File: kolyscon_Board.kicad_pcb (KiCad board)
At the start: 2 copper layers, 47 parts, among them J1 Conn_01x04, Q1 HL2302, Q10 HL2302, Q11 HL2302, Q2 HL2302, Q3 HL2302, Q4 HL2302, Q5 HL2302, Q6 HL2302, Q7 HL2302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

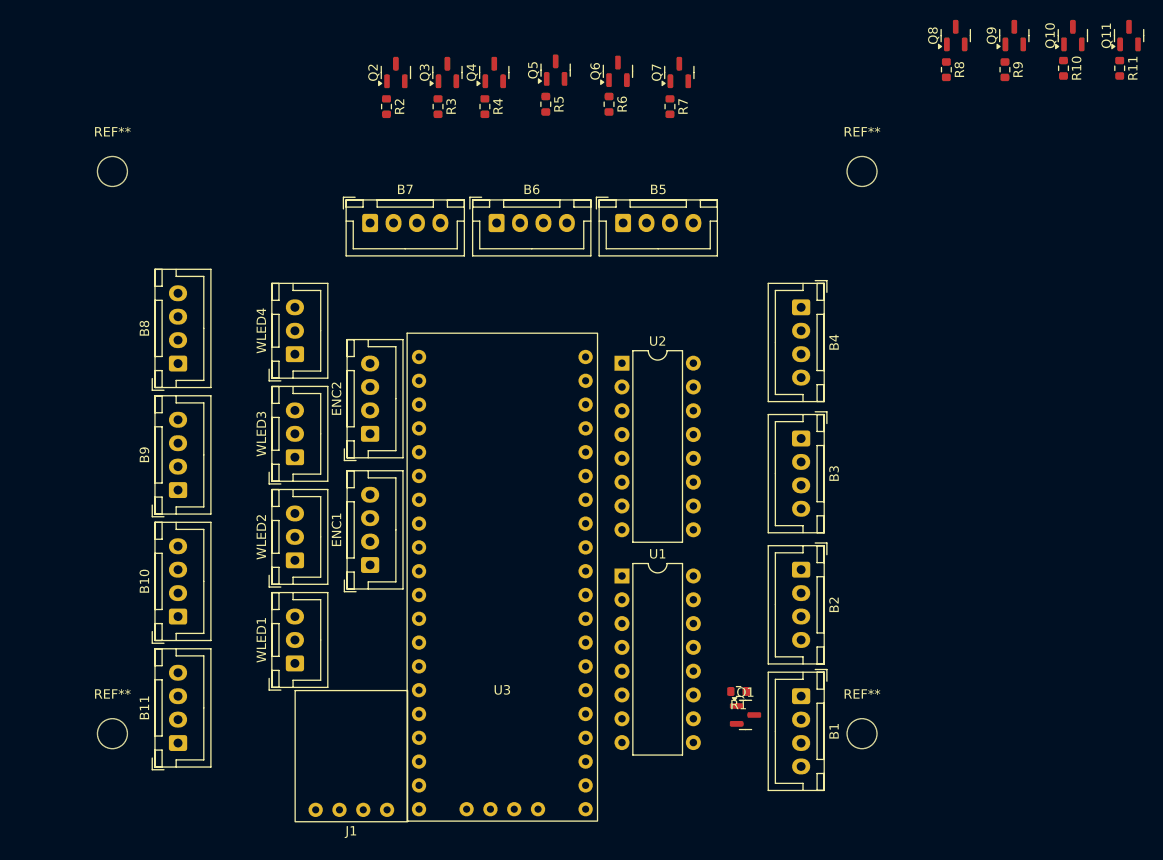
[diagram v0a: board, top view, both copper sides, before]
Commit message: Schema work
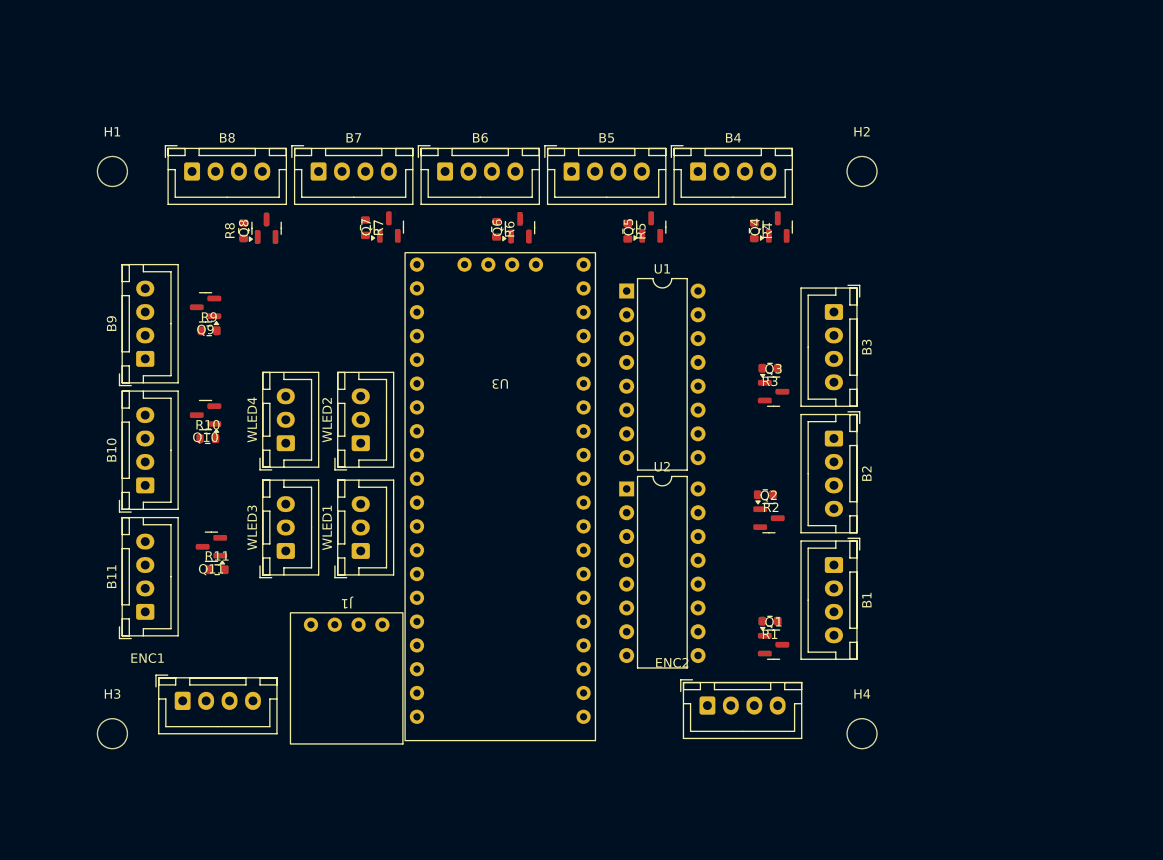
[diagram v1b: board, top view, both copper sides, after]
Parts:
- removed REF** (x4): MountingHole_3.2mm_M3, MountingHole:MountingHole_3.2mm_M3
- added H1: MountingHole, MountingHole:MountingHole_3.2mm_M3, F.Cu at (70.0, 70.0)
- added H2: MountingHole, MountingHole:MountingHole_3.2mm_M3, F.Cu at (150.0, 70.0)
- added H3: MountingHole, MountingHole:MountingHole_3.2mm_M3, F.Cu at (70.0, 130.0)
- added H4: MountingHole, MountingHole:MountingHole_3.2mm_M3, F.Cu at (150.0, 130.0)
- moved Q11 112.1 mm to (80.6, 110.0), turned to 180 degrees
- moved R11 110.2 mm to (81.2, 112.5), turned to 0 degrees
- moved Q10 101.0 mm to (79.9, 96.0), turned to 180 degrees
- moved R10 99.5 mm to (80.2, 98.5), turned to 0 degrees
- moved Q9 91.1 mm to (79.9, 84.5), turned to 180 degrees
- moved R9 89.4 mm to (80.3, 87.0), turned to 0 degrees
- moved R8 76.9 mm to (84.0, 76.3), turned to 90 degrees
- moved Q8 76.4 mm to (86.5, 76.1)
- moved Q2 62.0 mm to (140.1, 107.0), turned to 0 degrees
- moved U3 60.7 mm to (111.4, 78.7), turned to 180 degrees
- moved R2 57.9 mm to (139.7, 104.5), turned to 180 degrees
- moved Q3 48.7 mm to (140.6, 93.5), turned to 0 degrees
- moved ENC2 46.2 mm to (133.5, 127.0), turned to 0 degrees
- moved R3 45.1 mm to (140.2, 91.0), turned to 180 degrees
- moved Q7 35.1 mm to (99.5, 75.9)
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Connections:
- J1 pad 1: GND -> GND_PWR
- WLED1 pad 1: GND -> GND_PWR
- WLED2 pad 1: GND -> GND_PWR
- WLED3 pad 1: GND -> GND_PWR
- WLED4 pad 1: GND -> GND_PWR

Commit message: -Routing
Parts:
- added G***: LOGO, kolyscon_Board_Footprints:konmai, F.Cu at (92.0, 83.0)
- Q1, Q10, Q11, Q2, Q3, Q4, Q5, Q6, Q7, Q8, Q9: value HL2302 -> ~
- R1, R10, R11, R2, R3, R4, R5, R6, R7, R8, R9: value R -> R1k
- moved WLED4 8.63 mm to (97.0, 97.5)
- moved WLED3 8.50 mm to (97.0, 110.5)
- moved WLED2 7.65 mm to (89.0, 97.5)
- moved WLED1 7.50 mm to (89.0, 110.5)
- moved Q9 3.25 mm to (79.9, 81.2)
- moved R9 3.25 mm to (80.3, 83.8)
- moved B1 2.50 mm to (147.0, 109.5)
- moved B2 2.50 mm to (147.0, 96.0)
- moved B3 2.50 mm to (147.0, 82.5)
- moved Q1 2.50 mm to (140.6, 118.0)
- moved Q2 2.50 mm to (140.1, 104.5)
- moved Q3 2.50 mm to (140.6, 91.0)
- moved R1 2.50 mm to (140.2, 115.5)
- moved R2 2.50 mm to (139.7, 102.0)
- moved R3 2.50 mm to (140.2, 88.5)
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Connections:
- J1 pad 1: GND_PWR -> GND
- U3 pad 10: /BT_D_6 -> /BT_D_2
- U3 pad 11: /BT_D_7 -> /BT_D_3
- U3 pad 12: /BT_D_8 -> /BT_D_4
- U3 pad 13: /BT_D_9 -> /BT_D_7
- U3 pad 14: /BT_D_10 -> /BT_D_6
- U3 pad 15: unconnected-(U3-GND-Pad15) -> GND
- U3 pad 16: /BT_D_11 -> /BT_D_5
- U3 pad 25: /WLED_1 -> /BT_D_8
- U3 pad 26: /WLED_2 -> /BT_D_9
- U3 pad 27: /WLED_3 -> /BT_D_10
- U3 pad 28: /WLED_4 -> /BT_D_11
- U3 pad 29: /ENC_1_A -> /WLED_1
- U3 pad 30: /ENC_1_B -> /WLED_2
- U3 pad 31: /ENC_2_A -> /WLED_3
- U3 pad 32: /ENC_2_B -> /WLED_4
- U3 pad 4: /BT_D_1 -> /ENC_1_A
- U3 pad 5: /BT_D_2 -> /ENC_1_B
- U3 pad 6: unconnected-(U3-GND-Pad6) -> GND
- U3 pad 7: /BT_D_4 -> /ENC_2_A
- U3 pad 8: /BT_D_3 -> /ENC_2_B
- U3 pad 9: /BT_D_5 -> /BT_D_1
- WLED1 pad 1: GND_PWR -> GND
- WLED2 pad 1: GND_PWR -> GND
- WLED3 pad 1: GND_PWR -> GND
- WLED4 pad 1: GND_PWR -> GND
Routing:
- net GND: track 0.00 -> 486.9 mm
- net +5V: track 0.00 -> 348.2 mm, vias 0 -> 2
- net /BT_L_9: track 0.00 -> 62.5 mm, vias 0 -> 2
- net /BT_D_11: track 0.00 -> 52.4 mm
- net /BT_L_11: track 0.00 -> 49.6 mm, vias 0 -> 1
- net /BT_L_8: track 0.00 -> 48.7 mm, vias 0 -> 2
- net /SHIFTREG_SER: track 0.00 -> 48.6 mm
- net /BT_L_10: track 0.00 -> 48.0 mm, vias 0 -> 3
- net /SHIFTREG_LATCH: track 0.00 -> 45.8 mm, vias 0 -> 2
- net /BT_D_7: track 0.00 -> 45.7 mm
- net /ENC_1_A: track 0.00 -> 45.6 mm, vias 0 -> 1
- net /ENC_1_B: track 0.00 -> 43.8 mm
- net +5V_PWR: track 0.00 -> 43.6 mm
- net /SHIFTREG_CLK: track 0.00 -> 43.5 mm, vias 0 -> 2
- net /BT_D_3: track 0.00 -> 42.9 mm
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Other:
- board outline added: 88 x 68.5 mm
- board text added: "A"
- board text added: "B"
- board text added: "BT"
- board text added: "D"
- board text added: "GND"
- board text added: "LEDV0"
- board text added: "PURE"
- board text added: "QUALITY"
- board text added: "VCC"

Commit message: Routing refactors
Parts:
- moved U2 22.7 mm to (125.7, 80.5)
- moved U1 21.8 mm to (125.7, 103.1)
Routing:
- net GND: track 486.9 -> 0.12 mm
- net /SHIFTREG_SER: track 48.6 -> 0.00 mm
- net /SHIFTREG_LATCH: track 45.8 -> 0.00 mm, vias 2 -> 0
- net /SHIFTREG_CLK: track 43.5 -> 0.00 mm, vias 2 -> 0
- net /BT_L_1: track 38.7 -> 12.4 mm, vias 4 -> 1
- net /BT_L_4: track 17.8 -> 41.8 mm
- net /BT_L_5: track 14.1 -> 36.3 mm
- net /BT_L_8: track 48.7 -> 68.8 mm, vias 2 -> 1
- net /BT_L_6: track 24.4 -> 43.5 mm
- net /BT_L_11: track 49.6 -> 68.3 mm, vias 1 -> 3
- net /BT_L_2: track 33.1 -> 14.7 mm, vias 5 -> 0
- net /BT_L_7: track 38.0 -> 55.3 mm
- net Net-(U1-QH'): track 11.0 -> 0.00 mm
- net /BT_L_3: track 17.2 -> 28.1 mm, vias 2 -> 3
- net /BT_L_10: track 48.0 -> 55.3 mm, vias 3 -> 4
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
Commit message: V1 finalization
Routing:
- net +5V: track 346.8 -> 0.00 mm
- net /SHIFTREG_LATCH: track 0.00 -> 47.8 mm, vias 0 -> 1
- net /SHIFTREG_CLK: track 0.00 -> 46.3 mm, vias 0 -> 1
- net Net-(U1-QH'): track 0.00 -> 40.9 mm, vias 0 -> 3
- net /SHIFTREG_SER: track 0.00 -> 30.2 mm, vias 0 -> 1
- net Net-(Q6-G): track 0.00 -> 2.64 mm
- net /ENC_1_A: track 46.2 -> 48.3 mm
- net /BT_L_1: track 12.4 -> 13.8 mm
- net Net-(B3-Pin_2): track 9.53 -> 8.28 mm
- net /BT_D_6: track 32.2 -> 31.0 mm
- net /BT_L_11: track 68.3 -> 69.3 mm
- net /WLED_2: track 15.5 -> 14.5 mm
- net Net-(B4-Pin_2): track 9.11 -> 8.36 mm
- net /BT_L_3: track 28.1 -> 27.4 mm, vias 3 -> 2
- net /BT_L_9: track 60.9 -> 61.5 mm
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- added copper zone on B.Cu, net +5V
- added copper zone on F.Cu, net GND
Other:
- board text added: "Free design and software"
- board text added: "Kolyscon_Board V1.0"
- board text added: "github.com/Kolyasisan"

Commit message: Some refactors and fixes
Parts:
- Q1, Q10, Q11, Q2, Q3, Q4, Q5, Q6, Q7, Q8, Q9: footprint Package_TO_SOT_SMD:SOT-23 -> Package_TO_SOT_SMD:SOT-23-3
- R1, R10, R11, R2, R3, R4, R5, R6, R7, R8, R9: value R1k -> R2k
- moved ENC2 2.10 mm to (135.6, 127.0)
- moved J1 1.00 mm to (94.0, 116.1)
- moved ENC1 0.50 mm to (77.0, 126.5)
- moved Q4 0.06 mm to (141.0, 76.0)
- moved Q5 0.06 mm to (127.5, 76.0)
- moved Q7 0.06 mm to (99.5, 76.0)
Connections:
- U1 pad 10: +5V -> +3.3V
- U1 pad 16: +5V -> +3.3V
- U2 pad 10: +5V -> +3.3V
- U2 pad 16: +5V -> +3.3V
- U3 pad 40: unconnected-(U3-3V3-Pad40) -> +3.3V
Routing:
- net +3.3V: track 0.00 -> 87.9 mm, vias 0 -> 3
- net /ENC_2_B: track 27.8 -> 30.5 mm
- net /ENC_2_A: track 23.6 -> 25.7 mm
- net /BT_L_11: track 69.3 -> 68.7 mm
- net /ENC_1_B: track 43.8 -> 44.3 mm
- net /BT_L_3: vias 2 -> 1
- net /BT_L_9: vias 4 -> 2
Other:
- board text added: "Kolyscon_Board V1.1"
- board text removed: "Kolyscon_Board V1.0"

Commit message: Board refactors and fixes
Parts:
- Q1, Q10, Q11, Q2, Q3, Q4, Q5, Q6, Q7, Q8, Q9: footprint Package_TO_SOT_SMD:SOT-23-3 -> Package_TO_SOT_THT:TO-92_Inline
- R1, R10, R11, R2, R3, R4, R5, R6, R7, R8, R9: footprint Resistor_SMD:R_0603_1608Metric -> Resistor_THT:R_Axial_DIN0204_L3.6mm_D1.6mm_P1.90mm_Vertical
- moved R11 2.76 mm to (79.5, 113.3)
- moved R9 2.63 mm to (79.7, 86.3)
- moved R10 2.60 mm to (79.4, 99.8)
- moved R5 2.50 mm to (122.7, 75.4)
- moved R3 2.45 mm to (141.0, 86.2)
- moved R4 2.44 mm to (136.2, 75.5)
- moved Q10 2.43 mm to (80.3, 97.1), turned to 90 degrees
- moved Q11 2.38 mm to (80.3, 110.6), turned to 90 degrees
- moved R2 2.34 mm to (140.7, 99.9)
- moved Q9 2.32 mm to (80.5, 83.5), turned to 90 degrees
- moved R1 2.31 mm to (140.9, 113.3)
- moved Q1 2.12 mm to (140.1, 115.9), turned to -90 degrees
- moved Q3 2.11 mm to (140.1, 88.9), turned to -90 degrees
- moved R8 2.11 mm to (82.2, 75.4)
- moved Q4 2.11 mm to (138.9, 76.4), turned to 0 degrees
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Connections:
- Q1 pad 1: Net-(Q1-G) -> Net-(B1-Pin_2)
- Q1 pad 2: GND -> Net-(Q1-B)
- Q1 pad 3: Net-(B1-Pin_2) -> GND
- Q10 pad 1: Net-(Q10-G) -> Net-(B10-Pin_2)
- Q10 pad 2: GND -> Net-(Q10-S)
- Q10 pad 3: Net-(B10-Pin_2) -> GND
- Q11 pad 1: Net-(Q11-G) -> Net-(B11-Pin_2)
- Q11 pad 2: GND -> Net-(Q11-S)
- Q11 pad 3: Net-(B11-Pin_2) -> GND
- Q2 pad 1: Net-(Q2-G) -> Net-(B2-Pin_2)
- Q2 pad 2: GND -> Net-(Q2-S)
- Q2 pad 3: Net-(B2-Pin_2) -> GND
- Q3 pad 1: Net-(Q3-G) -> Net-(B3-Pin_2)
- Q3 pad 2: GND -> Net-(Q3-S)
- Q3 pad 3: Net-(B3-Pin_2) -> GND
- Q4 pad 1: Net-(Q4-G) -> Net-(B4-Pin_2)
- Q4 pad 2: GND -> Net-(Q4-S)
- Q4 pad 3: Net-(B4-Pin_2) -> GND
- Q5 pad 1: Net-(Q5-G) -> Net-(B5-Pin_2)
- Q5 pad 2: GND -> Net-(Q5-S)
- Q5 pad 3: Net-(B5-Pin_2) -> GND
- Q6 pad 1: Net-(Q6-G) -> Net-(B6-Pin_2)
- Q6 pad 2: GND -> Net-(Q6-S)
- Q6 pad 3: Net-(B6-Pin_2) -> GND
- Q7 pad 1: Net-(Q7-G) -> Net-(B7-Pin_2)
- Q7 pad 2: GND -> Net-(Q7-S)
- Q7 pad 3: Net-(B7-Pin_2) -> GND
- Q8 pad 1: Net-(Q8-G) -> Net-(B8-Pin_2)
- Q8 pad 2: GND -> Net-(Q8-S)
- Q8 pad 3: Net-(B8-Pin_2) -> GND
- Q9 pad 1: Net-(Q9-G) -> Net-(B9-Pin_2)
- Q9 pad 2: GND -> Net-(Q9-S)
- Q9 pad 3: Net-(B9-Pin_2) -> GND
- R1 pad 1: Net-(Q1-G) -> Net-(Q1-B)
- R10 pad 1: Net-(Q10-G) -> Net-(Q10-S)
- R11 pad 1: Net-(Q11-G) -> Net-(Q11-S)
- R2 pad 1: Net-(Q2-G) -> Net-(Q2-S)
- R3 pad 1: Net-(Q3-G) -> Net-(Q3-S)
- R4 pad 1: Net-(Q4-G) -> Net-(Q4-S)
- R5 pad 1: Net-(Q5-G) -> Net-(Q5-S)
- R6 pad 1: Net-(Q6-G) -> Net-(Q6-S)
- R7 pad 1: Net-(Q7-G) -> Net-(Q7-S)
- R8 pad 1: Net-(Q8-G) -> Net-(Q8-S)
- R9 pad 1: Net-(Q9-G) -> Net-(Q9-S)
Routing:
- net Net-(Q4-S): track 0.00 -> 6.44 mm
- net Net-(Q9-S): track 0.00 -> 5.79 mm
- net Net-(Q11-S): track 0.00 -> 5.77 mm
- net Net-(Q7-S): track 0.00 -> 5.75 mm
- net Net-(Q3-S): track 0.00 -> 5.72 mm
- net Net-(Q2-S): track 0.00 -> 5.64 mm
- net Net-(Q5-S): track 0.00 -> 5.63 mm
- net Net-(Q8-S): track 0.00 -> 5.62 mm
- net Net-(Q6-S): track 0.00 -> 5.58 mm
- net Net-(Q1-B): track 0.00 -> 5.50 mm
- net Net-(Q10-S): track 0.00 -> 5.34 mm
- net Net-(Q10-G): track 2.81 -> 0.00 mm
- net Net-(Q6-G): track 2.64 -> 0.00 mm
- net Net-(Q7-G): track 2.63 -> 0.00 mm
- net Net-(Q9-G): track 2.60 -> 0.00 mm
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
